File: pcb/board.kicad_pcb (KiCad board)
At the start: 4 copper layers, 159.9 x 99.9 mm, 158 parts, among them J1 Conn_02x03_Counter_Clockwise, J2 USB_B, J3 650913-5, SW1 SW_Push, U1 XC6SLX9-TQG144, U10 LTC3633EFEPBF, U11 74LVC1G08, U12 IS61WV25616EFBLL, U14 ECS-7050MV, U15 BCM56DS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

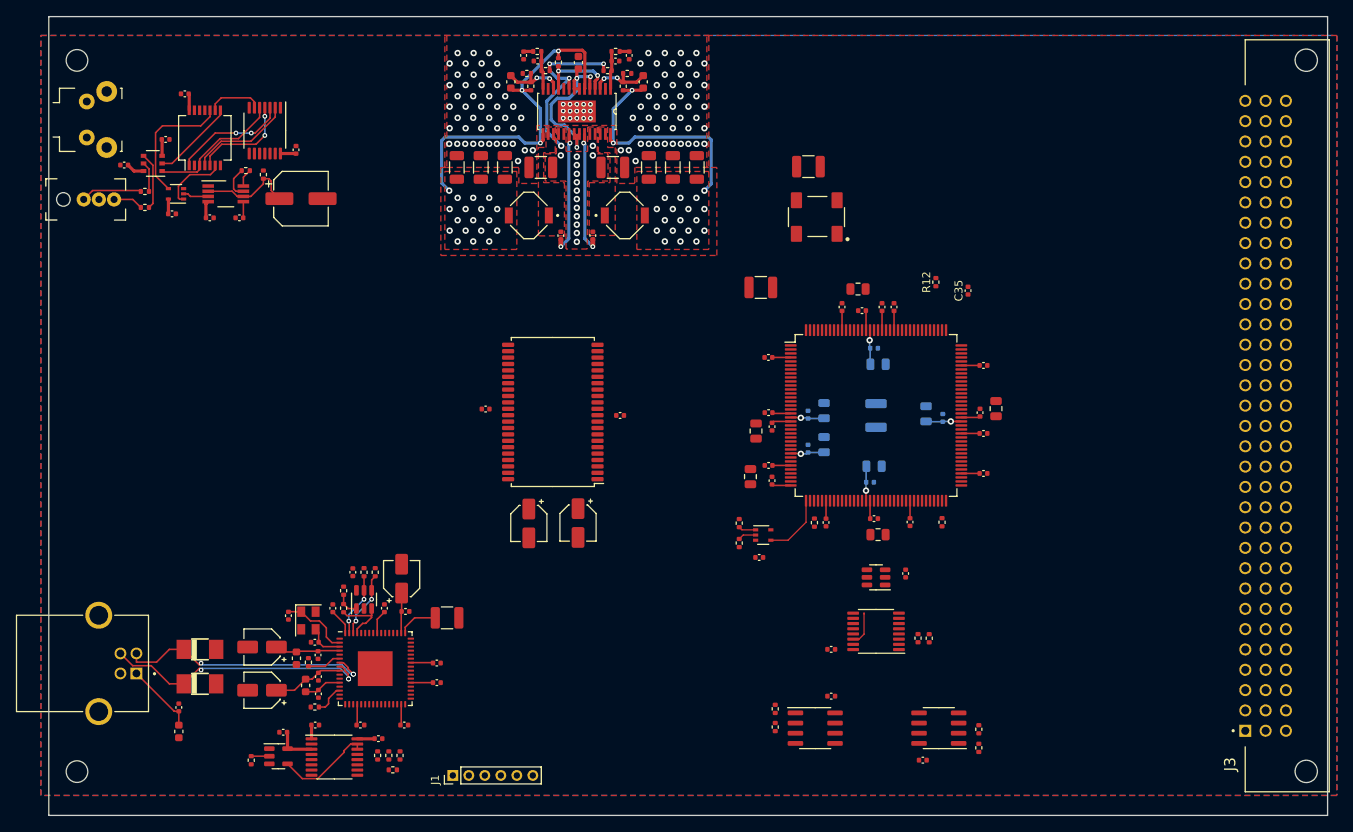
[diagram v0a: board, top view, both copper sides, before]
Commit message: added silkscreen values
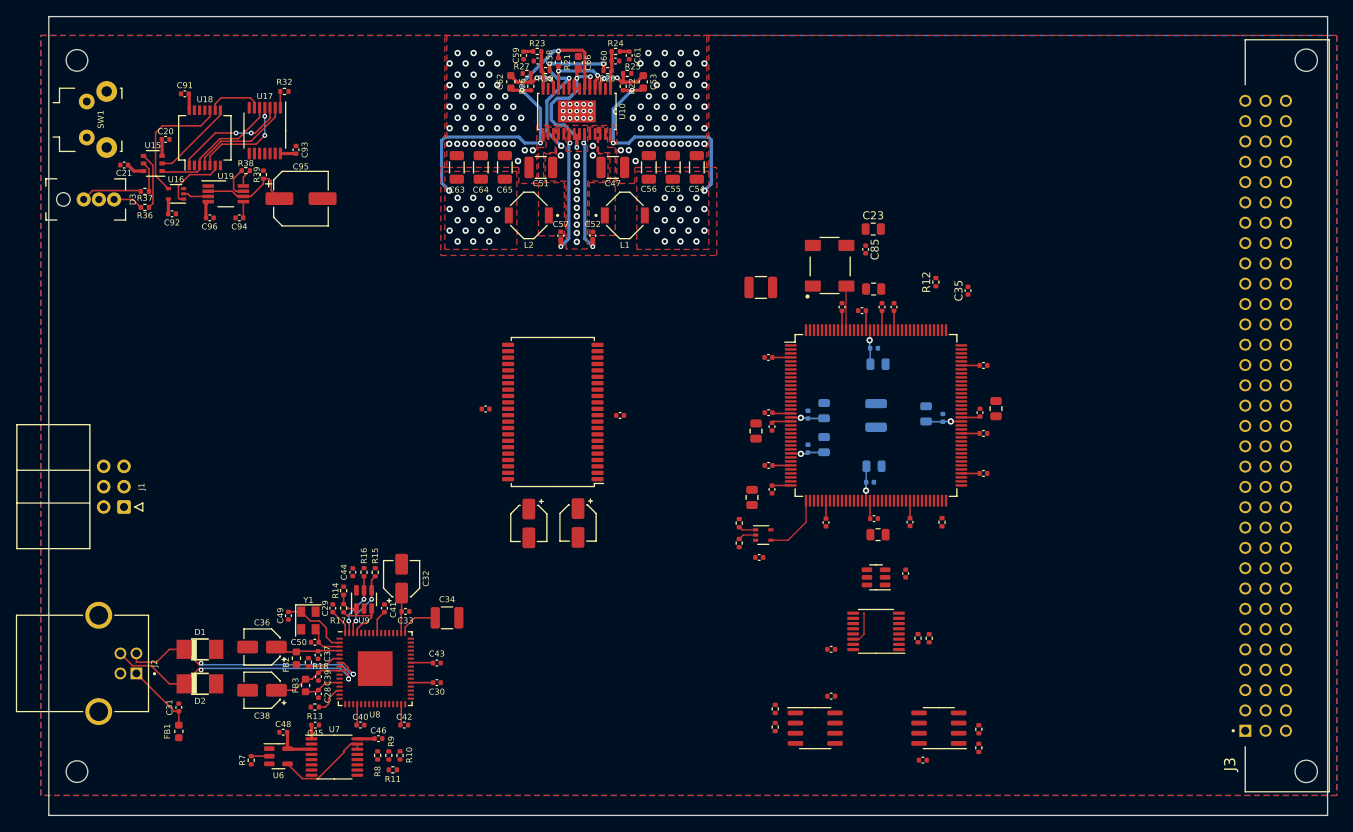
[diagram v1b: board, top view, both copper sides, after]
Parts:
- removed C90: 100uF, Capacitor_SMD:C_1210_3225Metric
- added C23: 4.7uF, Capacitor_SMD:C_0805_2012Metric, F.Cu at (158.1, 71.6)
- added C85: 470nF, Capacitor_SMD:C_0402_1005Metric, F.Cu at (157.2, 74.2)
- J1: footprint Connector_PinHeader_2.00mm:PinHeader_1x06_P2.00mm_Vertical -> Connector_IDC:IDC-Header_2x03_P2.54mm_Horizontal
- moved R32 85.4 mm to (84.5, 54.4), turned to 0 degrees
- moved J1 53.1 mm to (64.5, 106.4), turned to 180 degrees
- moved U14 7.20 mm to (150.6, 78.8), turned to 90 degrees
- moved C81 2.61 mm to (143.0, 105.2), turned to -90 degrees
- moved C7 1.95 mm to (158.2, 79.1), turned to 0 degrees
- moved C9 1.10 mm to (145.5, 104.2), turned to -90 degrees
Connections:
- U1 pad 1: unconnected-(U1-Pad1) -> SRAM_A6
- U1 pad 10: unconnected-(U1-Pad10) -> SRAM_IO6
- U1 pad 11: unconnected-(U1-Pad11) -> SRAM_IO9
- U1 pad 12: unconnected-(U1-Pad12) -> SRAM_IO5
- U1 pad 134: unconnected-(U1-Pad134) -> Net-(U1-Pad134)
- U1 pad 138: unconnected-(U1-Pad138) -> SRAM_A9
- U1 pad 139: unconnected-(U1-Pad139) -> SRAM_A10
- U1 pad 14: unconnected-(U1-Pad14) -> SRAM_IO10
- U1 pad 140: unconnected-(U1-Pad140) -> SRAM_A8
- U1 pad 141: unconnected-(U1-Pad141) -> SRAM_A11
- U1 pad 142: unconnected-(U1-Pad142) -> SRAM_A7
- U1 pad 143: unconnected-(U1-Pad143) -> SRAM_A12
- U1 pad 15: unconnected-(U1-Pad15) -> SRAM_IO4
- U1 pad 16: unconnected-(U1-Pad16) -> SRAM_IO11
- U1 pad 17: unconnected-(U1-Pad17) -> SRAM_IO3
- U1 pad 2: unconnected-(U1-Pad2) -> SRAM_A13
- U1 pad 21: unconnected-(U1-Pad21) -> SRAM_IO12
- U1 pad 22: unconnected-(U1-Pad22) -> SRAM_IO2
- U1 pad 23: unconnected-(U1-Pad23) -> SRAM_IO13
- U1 pad 24: unconnected-(U1-Pad24) -> SRAM_IO1
- U1 pad 26: unconnected-(U1-Pad26) -> SRAM_IO14
- U1 pad 27: unconnected-(U1-Pad27) -> SRAM_IO0
- U1 pad 29: unconnected-(U1-Pad29) -> SRAM_IO15
- U1 pad 30: unconnected-(U1-Pad30) -> SRAM_CS#
- U1 pad 32: unconnected-(U1-Pad32) -> SRAM_A4
- U1 pad 33: unconnected-(U1-Pad33) -> SRAM_A3
- U1 pad 34: unconnected-(U1-Pad34) -> SRAM_A2
- U1 pad 35: unconnected-(U1-Pad35) -> SRAM_A15
- U1 pad 40: unconnected-(U1-Pad40) -> SRAM_A1
- U1 pad 41: unconnected-(U1-Pad41) -> SRAM_A16
- U1 pad 43: unconnected-(U1-Pad43) -> FPGA_SPI_ROM_CS
- U1 pad 44: unconnected-(U1-Pad44) -> SRAM_A0
- U1 pad 45: unconnected-(U1-Pad45) -> SRAM_A17
- U1 pad 5: unconnected-(U1-Pad5) -> SRAM_A5
- U1 pad 56: FPGA_SPI_ROM_CS -> unconnected-(U1-Pad56)
- U1 pad 6: unconnected-(U1-Pad6) -> SRAM_A14
- U1 pad 7: unconnected-(U1-Pad7) -> SRAM_WE#
- U1 pad 8: unconnected-(U1-Pad8) -> SRAM_IO7
- U1 pad 9: unconnected-(U1-Pad9) -> SRAM_IO8
- U12 pad 39: SRAM_LB# -> GND
- U12 pad 40: SRAM_UB# -> GND
- U12 pad 41: SRAM_OE# -> GND
- U14 pad 3: unconnected-(U14-Pad3) -> Net-(U1-Pad134)
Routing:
- net Net-(U1-Pad134): track 0.00 -> 5.53 mm
- net INIT_B#: track 0.00 -> 2.04 mm

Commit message: route the sram
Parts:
- C14, C78, C81: moved to B.Cu
- moved C67 28.8 mm to (121.1, 80.2), turned to 90 degrees
- moved C70 28.8 mm to (115.0, 80.3), turned to 90 degrees
- moved C71 10.3 mm to (133.6, 113.2)
- moved R34 10.3 mm to (131.1, 108.9)
- moved R35 10.3 mm to (131.1, 111.4)
- moved U11 10.3 mm to (134.1, 110.4)
- moved C81 7.97 mm to (150.5, 102.5), turned to 90 degrees
- moved C14 5.05 mm to (152.7, 103.3), turned to 0 degrees
- moved C78 2.32 mm to (142.2, 94.9), turned to 180 degrees
- moved C8 0.64 mm to (145.0, 95.9), turned to 180 degrees
- moved C19 0.15 mm to (145.1, 94.7)
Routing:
- net SRAM_A14: track 0.00 -> 48.4 mm, vias 0 -> 2
- net SRAM_IO10: track 0.00 -> 48.3 mm, vias 0 -> 2
- net SRAM_IO12: track 0.00 -> 48.3 mm, vias 0 -> 2
- net SRAM_IO13: track 0.00 -> 48.3 mm, vias 0 -> 2
- net SRAM_A13: track 0.00 -> 48.3 mm, vias 0 -> 2
- net SRAM_IO11: track 0.00 -> 48.3 mm, vias 0 -> 2
- net SRAM_A17: track 0.00 -> 48.2 mm, vias 0 -> 2
- net SRAM_A12: track 0.00 -> 46.9 mm, vias 0 -> 2
- net SRAM_A10: track 0.00 -> 46.9 mm, vias 0 -> 2
- net SRAM_A11: track 0.00 -> 46.9 mm, vias 0 -> 2
- net SRAM_A15: track 0.00 -> 46.9 mm, vias 0 -> 2
- net SRAM_A16: track 0.00 -> 46.6 mm, vias 0 -> 2
- net SRAM_IO14: track 0.00 -> 45.7 mm, vias 0 -> 2
- net SRAM_IO8: track 0.00 -> 45.5 mm, vias 0 -> 2
- net SRAM_IO9: track 0.00 -> 45.4 mm, vias 0 -> 2
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
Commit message: route the sram
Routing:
- net USB_SPI_MISO: track 0.00 -> 70.4 mm
- net USB_SPI_MOSI: track 0.00 -> 64.8 mm
- net USB_SPI_CLK: track 0.00 -> 63.5 mm
- net USB_SPI_CONFIG_CS: track 0.00 -> 62.5 mm
- net USB_SPI_ROM_CS: track 4.36 -> 56.3 mm
- net SRAM_WE#: track 24.5 -> 52.4 mm
- net SRAM_CS#: track 24.9 -> 52.2 mm
- net SRAM_IO11: track 48.3 -> 39.7 mm
- net SRAM_A13: track 48.3 -> 41.1 mm
- net SRAM_IO12: track 48.3 -> 41.3 mm
- net SRAM_IO13: track 48.3 -> 41.7 mm
- net SRAM_A14: track 48.4 -> 42.8 mm
- net SRAM_IO10: track 48.3 -> 43.1 mm
- net SRAM_A15: track 46.9 -> 42.6 mm
- net SRAM_IO8: track 45.5 -> 42.4 mm
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
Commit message: keep routing the flash
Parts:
- moved R1 20.5 mm to (150.2, 138.1)
- moved R4 20.5 mm to (151.6, 138.1)
- moved R35 10.9 mm to (141.8, 112.9)
- moved U11 10.9 mm to (144.8, 111.9)
- moved C71 10.9 mm to (144.3, 114.7)
- moved R34 10.9 mm to (141.8, 110.4)
- moved C27 0.30 mm to (161.9, 114.7)
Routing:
- net /Flash Memory/SPI_CLK: track 0.00 -> 30.8 mm
- net /Flash Memory/SPI_MOSI: track 0.00 -> 30.6 mm
- net /Flash Memory/SPI_ROM_CS: track 0.00 -> 28.1 mm, vias 0 -> 2
- net /Flash Memory/SPI_CONFIG_CS: track 0.00 -> 24.4 mm, vias 0 -> 2
- net VCCAUX: track 137.4 -> 152.9 mm
- net SPI_PROGRAM#: track 2.19 -> 13.3 mm, vias 0 -> 2
- net Net-(R6-Pad2): track 0.00 -> 2.53 mm
- net Net-(R3-Pad2): track 0.00 -> 2.53 mm
